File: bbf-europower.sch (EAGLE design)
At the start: 9 parts

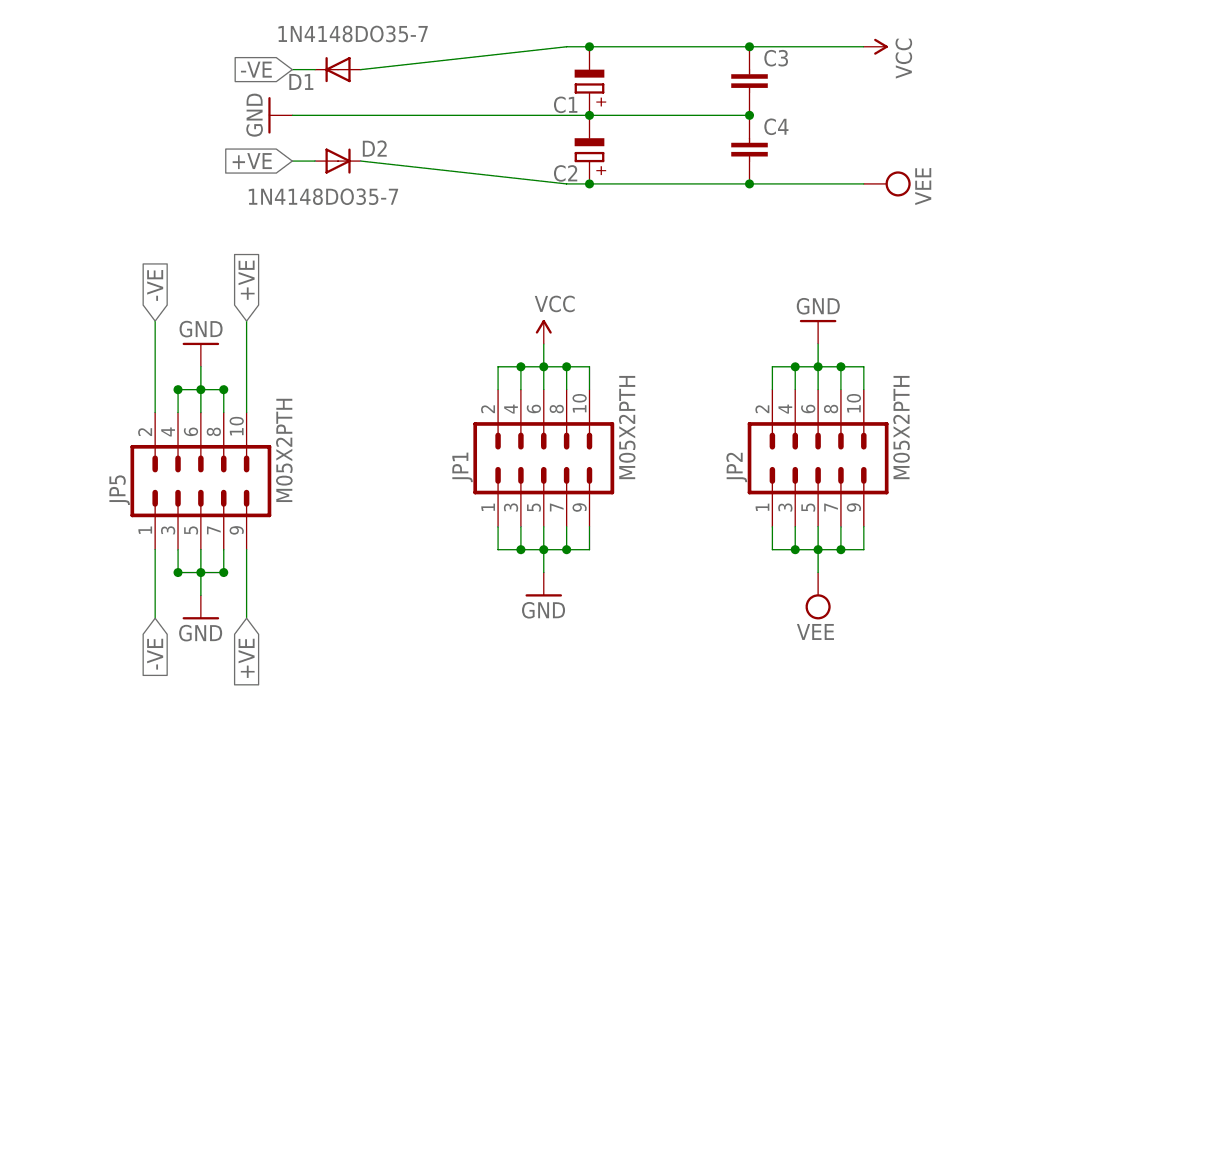
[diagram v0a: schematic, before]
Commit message: Add files via upload
Through-hole versions of Thomas Hopman's revision of the bbf-europower.
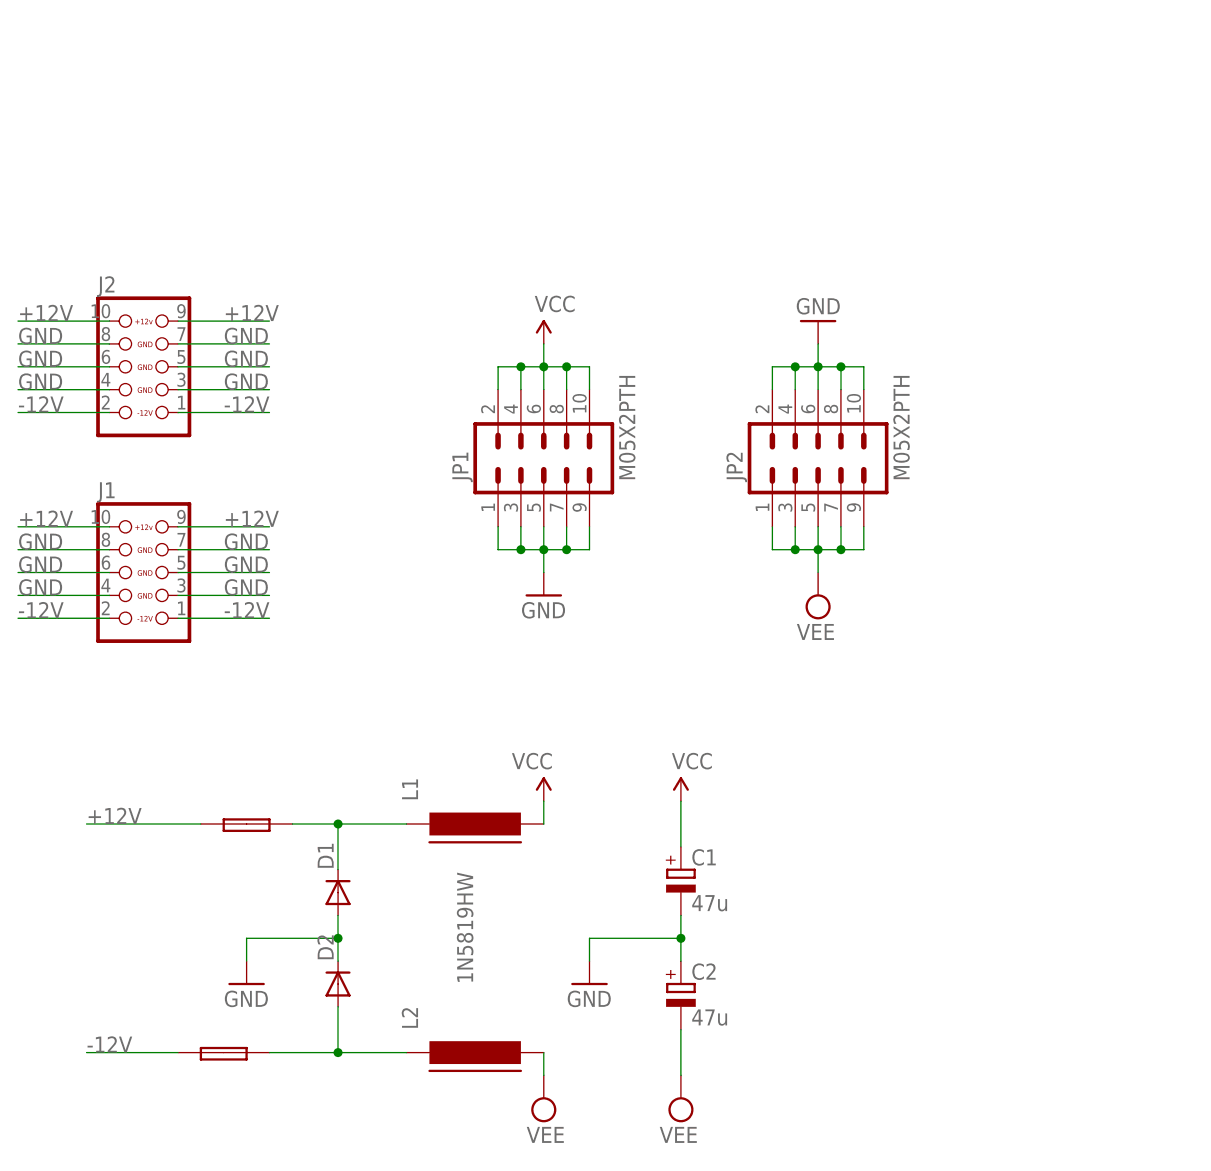
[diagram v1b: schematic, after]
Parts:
- removed C3, C4: (no value), TomW:C-EU025-025X050
- removed JP5: M05X2PTH, SparkFun:M05X2PTH
- added +FUSE1: +FUSE, TomW:PTC_FUSEPOLY_FUSE
- added -FUSE1: -FUSE, TomW:PTC_FUSEPOLY_FUSE
- added J1, J2: CON_HEADER_2X05-PTH, tomatek:CON_HEADER_2X05-PTH
- added L1, L2: (no value), GazJ:FERRITE-SHORT
- C1, C2: value (none) -> 47u; device resistor:CPOL-EUE2,5-6E -> resistor:CPOL-EUE2-5
- D1, D2: value 1N4148DO35-7 -> 1N5819HW
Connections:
- removed net +VE: D2.A, JP5.10, JP5.9
- removed net -VE: D1.C, JP5.1, JP5.2
- removed net N$10: JP5.4, JP5.8
- removed net N$5: JP5.3, JP5.7
- new net +12V: +FUSE1.P$1, J1.10, J1.9, J2.10, J2.9
- new net -12V: -FUSE1.P$1, J1.1, J1.2, J2.1, J2.2
- new net N$38: +FUSE1.P$2, D1.C, L1.1
- new net N$39: -FUSE1.P$2, D2.A, L2.1
- net GND: now also C1.-, C2.+, D1.A, D2.C, J1.3, J1.4, J1.5, J1.6, J1.7, J1.8, J2.3, J2.4, J2.5, J2.6, J2.7, J2.8; no longer C1.+, C2.-, C3.2, C4.1, JP5.5, JP5.6
- net VCC: now also C1.+, L1.2; no longer C1.-, C3.1, D1.A
- net VEE: now also C2.-, L2.2; no longer C2.+, C4.2, D2.C
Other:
- moved on the sheet: C1, C2, D1, D2

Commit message: adding the new 1x5 connector to ground - first attempt
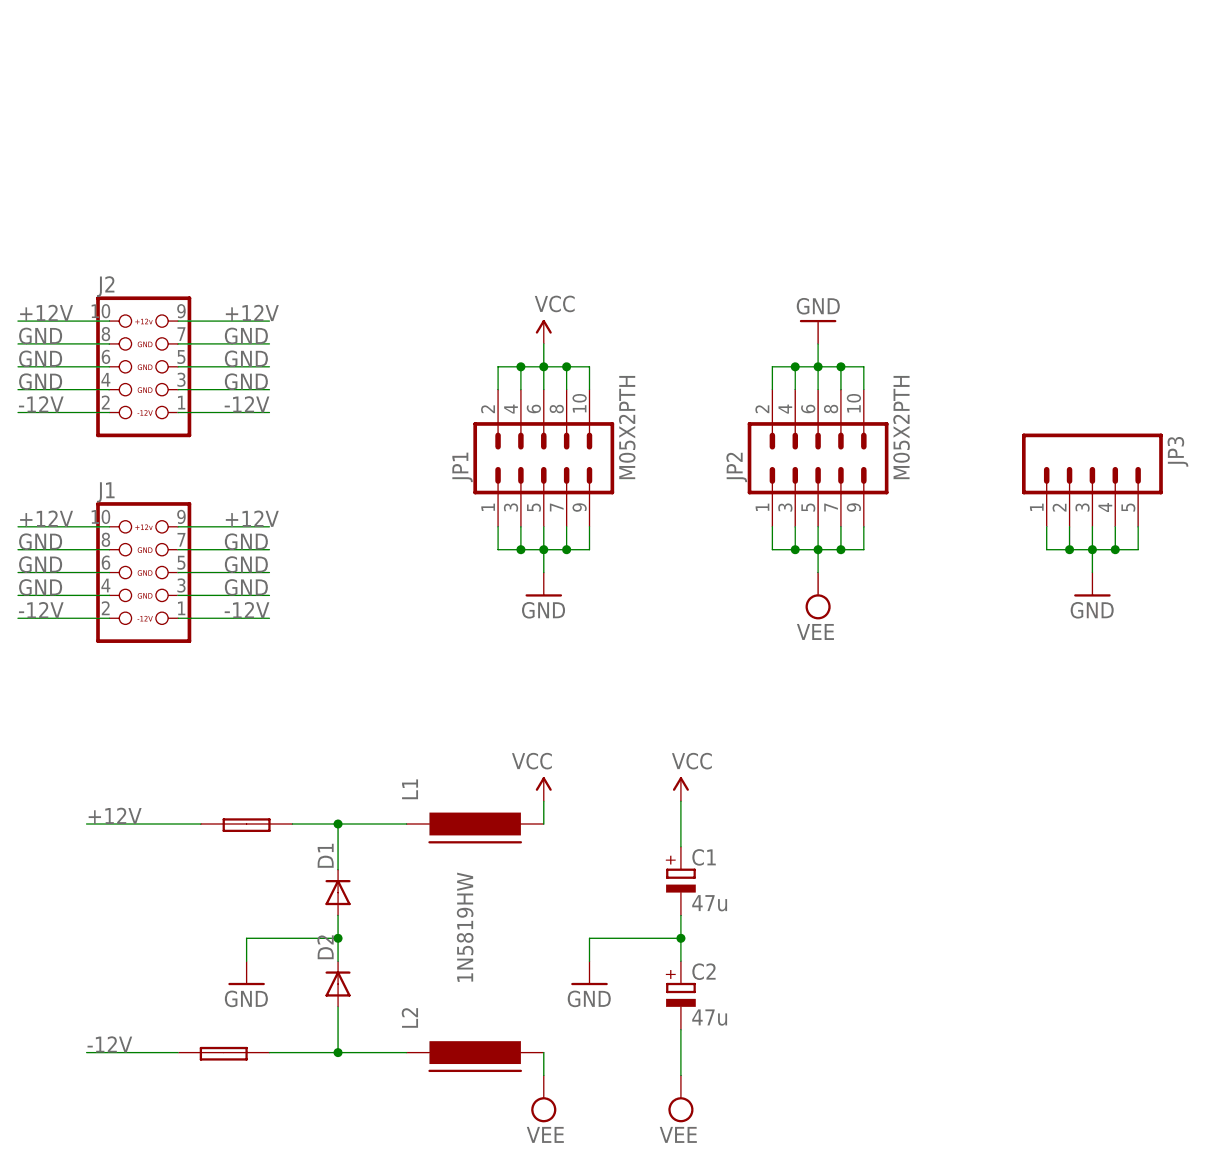
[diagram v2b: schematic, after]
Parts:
- added JP3: (no value), SparkFun:M05PTH
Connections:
- net GND: now also JP3.1, JP3.2, JP3.3, JP3.4, JP3.5
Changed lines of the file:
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@@
 <?xml version="1.0" encoding="utf-8"?>
 <!DOCTYPE eagle SYSTEM "eagle.dtd">
-<eagle version="7.3.0">
+<eagle version="9.6.2">
 <drawing>
 <settings>
-<setting alwaysvectorfont="yes"/>
+<setting alwaysvectorfont="no"/>
+<setting keepoldvectorfont="yes"/>
 <setting verticaltext="up"/>
 </settings>
@@
 <part name="+FUSE1" library="TomW" deviceset="PTC_FUSE" device="POLY_FUSE" value="+FUSE"/>
 <part name="-FUSE1" library="TomW" deviceset="PTC_FUSE" device="POLY_FUSE" value="-FUSE"/>
+<part name="JP3" library="SparkFun" deviceset="M05" device="PTH"/>
+<part name="GND5" library="SparkFun" deviceset="GND" device=""/>
 </parts>
 <sheets>
@@
 </plain>
 <instances>
-<instance part="GND2" gate="1" x="106.68" y="121.92"/>
-<instance part="GND4" gate="1" x="137.16" y="152.4" rot="R180"/>
-<instance part="SUPPLY2" gate="G$1" x="137.16" y="121.92" rot="R180"/>
-<instance part="P+1" gate="1" x="106.68" y="149.86"/>
-<instance part="JP1" gate="G$1" x="106.68" y="137.16" rot="R90"/>
-<instance part="JP2" gate="G$1" x="137.16" y="137.16" rot="R90"/>
-<instance part="J1" gate="J" x="58.42" y="124.46"/>
-<instance part="SUPPLY1" gate="G$1" x="106.68" y="66.04" rot="MR180"/>
-<instance part="P+2" gate="1" x="106.68" y="99.06" rot="MR0"/>
-<instance part="C1" gate="G$1" x="121.92" y="91.44"/>
-<instance part="C2" gate="G$1" x="121.92" y="78.74"/>
-<instance part="P+3" gate="1" x="121.92" y="99.06"/>
-<instance part="SUPPLY3" gate="G$1" x="121.92" y="66.04" rot="R180"/>
+<instance part="GND2" gate="1" x="106.68" y="121.92" smashed="yes">
+<attribute name="VALUE" x="104.14" y="119.38" size="1.778" layer="96"/>
+</instance>
+<instance part="GND4" gate="1" x="137.16" y="152.4" smashed="yes" rot="R180">
+<attribute name="VALUE" x="139.7" y="154.94" size="1.778" layer="96" rot="R180"/>
+</instance>
+<instance part="SUPPLY2" gate="G$1" x="137.16" y="121.92" smashed="yes" rot="R180">
+<attribute name="VALUE" x="139.065" y="118.745" size="1.778" layer="96" rot="R180"/>
+</instance>
+<instance part="P+1" gate="1" x="106.68" y="149.86" smashed="yes">
+<attribute name="VALUE" x="105.664" y="153.416" size="1.778" layer="96"/>
+</instance>
+<instance part="JP1" gate="G$1" x="106.68" y="137.16" smashed="yes" rot="R90">
+<attribute name="VALUE" x="116.84" y="134.62" size="1.778" layer="96" rot="R90"/>
+<attribute name="NAME" x="98.298" y="134.62" size="1.778" layer="95" rot="R90"/>
+</instance>
+<instance part="JP2" gate="G$1" x="137.16" y="137.16" smashed="yes" rot="R90">
+<attribute name="VALUE" x="147.32" y="134.62" size="1.778" layer="96" rot="R90"/>
+<attribute name="NAME" x="128.778" y="134.62" size="1.778" layer="95" rot="R90"/>
+</instance>
+<instance part="J1" gate="J" x="58.42" y="124.46" smashed="yes">
+<attribute name="NAME" x="57.15" y="132.715" size="1.778" layer="95"/>
+</instance>
+<instance part="SUPPLY1" gate="G$1" x="106.68" y="66.04" smashed="yes" rot="MR180">
+<attribute name="VALUE" x="104.775" y="62.865" size="1.778" layer="96" rot="MR180"/>
+</instance>
+<instance part="P+2" gate="1" x="106.68" y="99.06" smashed="yes" rot="MR0">
+<attribute name="VALUE" x="107.696" y="102.616" size="1.778" layer="96" rot="MR0"/>
+</instance>
+<instance part="C1" gate="G$1" x="121.92" y="91.44" smashed="yes">
+<attribute name="NAME" x="123.063" y="91.9226" size="1.778" layer="95"/>
+<attribute name="VALUE" x="123.063" y="86.8426" size="1.778" layer="96"/>
+</instance>
+<instance part="C2" gate="G$1" x="121.92" y="78.74" smashed="yes">
+<attribute name="NAME" x="123.063" y="79.2226" size="1.778" layer="95"/>
+<attribute name="VALUE" x="123.063" y="74.1426" size="1.778" layer="96"/>
+</instance>
+<instance part="P+3" gate="1" x="121.92" y="99.06" smashed="yes">
+<attribute name="VALUE" x="120.904" y="102.616" size="1.778" layer="96"/>
+</instance>
+<instance part="SUPPLY3" gate="G$1" x="121.92" y="66.04" smashed="yes" rot="R180">
+<attribute name="VALUE" x="123.825" y="62.865" size="1.778" layer="96" rot="R180"/>
+</instance>
 <instance part="D2" gate="G$1" x="83.82" y="78.74" smashed="yes" rot="R90">
 <attribute name="NAME" x="83.3374" y="81.28" size="1.778" layer="95" rot="R90"/>
@@
 <attribute name="NAME" x="83.3374" y="91.44" size="1.778" layer="95" rot="R90"/>
 </instance>
-<instance part="GND3" gate="1" x="111.76" y="78.74"/>
-<instance part="L1" gate="L" x="99.06" y="96.52" rot="R90"/>
-<instance part="L2" gate="L" x="99.06" y="71.12" rot="R90"/>
-<instance part="GND1" gate="1" x="73.66" y="78.74"/>
-<instance part="J2" gate="J" x="58.42" y="147.32"/>
-<instance part="+FUSE1" gate="G$1" x="73.66" y="96.52"/>
-<instance part="-FUSE1" gate="G$1" x="71.12" y="71.12"/>
+<instance part="GND3" gate="1" x="111.76" y="78.74" smashed="yes">
+<attribute name="VALUE" x="109.22" y="76.2" size="1.778" layer="96"/>
+</instance>
+<instance part="L1" gate="L" x="99.06" y="96.52" smashed="yes" rot="R90">
+<attribute name="NAME" x="92.71" y="99.06" size="1.778" layer="95" rot="R90"/>
+<attribute name="VALUE" x="105.41" y="99.06" size="1.778" layer="96" rot="R90"/>
+</instance>
+<instance part="L2" gate="L" x="99.06" y="71.12" smashed="yes" rot="R90">
+<attribute name="NAME" x="92.71" y="73.66" size="1.778" layer="95" rot="R90"/>
+<attribute name="VALUE" x="105.41" y="73.66" size="1.778" layer="96" rot="R90"/>
+</instance>
+<instance part="GND1" gate="1" x="73.66" y="78.74" smashed="yes">
+<attribute name="VALUE" x="71.12" y="76.2" size="1.778" layer="96"/>
+</instance>
+<instance part="J2" gate="J" x="58.42" y="147.32" smashed="yes">
+<attribute name="NAME" x="57.15" y="155.575" size="1.778" layer="95"/>
+</instance>
+<instance part="+FUSE1" gate="G$1" x="73.66" y="96.52" smashed="yes"/>
+<instance part="-FUSE1" gate="G$1" x="71.12" y="71.12" smashed="yes"/>
+<instance part="JP3" gate="G$1" x="167.64" y="137.16" smashed="yes" rot="R270">
+<attribute name="VALUE" x="157.48" y="139.7" size="1.778" layer="96" rot="R270"/>
+<attribute name="NAME" x="176.022" y="139.7" size="1.778" layer="95" rot="R270"/>
+</instance>
+<instance part="GND5" gate="1" x="167.64" y="121.92" smashed="yes">
+<attribute name="VALUE" x="165.1" y="119.38" size="1.778" layer="96"/>
+</instance>
 </instances>
 <busses>
@@
 <label x="48.26" y="144.78" size="1.778" layer="95"/>
 </segment>
+<segment>
+<pinref part="JP3" gate="G$1" pin="1"/>
+<wire x1="162.56" y1="129.54" x2="162.56" y2="127" width="0.1524" layer="91"/>
+<wire x1="162.56" y1="127" x2="165.1" y2="127" width="0.1524" layer="91"/>
+<pinref part="JP3" gate="G$1" pin="5"/>
+<wire x1="165.1" y1="127" x2="167.64" y2="127" width="0.1524" layer="91"/>
+<wire x1="167.64" y1="127" x2="170.18" y2="127" width="0.1524" layer="91"/>
+<wire x1="170.18" y1="127" x2="172.72" y2="127" width="0.1524" layer="91"/>
+<wire x1="172.72" y1="127" x2="172.72" y2="129.54" width="0.1524" layer="91"/>
+<pinref part="JP3" gate="G$1" pin="2"/>
+<wire x1="165.1" y1="129.54" x2="165.1" y2="127" width="0.1524" layer="91"/>
+<junction x="165.1" y="127"/>
+<pinref part="JP3" gate="G$1" pin="3"/>
+<wire x1="167.64" y1="129.54" x2="167.64" y2="127" width="0.1524" layer="91"/>
+<junction x="167.64" y="127"/>
+<pinref part="JP3" gate="G$1" pin="4"/>
+<wire x1="170.18" y1="129.54" x2="170.18" y2="127" width="0.1524" layer="91"/>
+<junction x="170.18" y="127"/>
+<pinref part="GND5" gate="1" pin="GND"/>
+<wire x1="167.64" y1="124.46" x2="167.64" y2="127" width="0.1524" layer="91"/>
+</segment>
 </net>
